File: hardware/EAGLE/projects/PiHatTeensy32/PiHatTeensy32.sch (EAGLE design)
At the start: 86 parts, among them IC2_0_PC JP, U0-C1 0.1uF, U0-C2 1nF, U0-C3 0.22uF, U0-C4 0.1uF, U0-C5 0.22uF, U0-R1 4.7k, U0-R2 47k, U0-R3 10k, U0-R4 10k, U1 TSR_1-2450, U1-C1 0.1uF, U1-C2 1nF, U1-C3 0.22uF, U1-C4 0.1uF, U1-C5 0.22uF, U1-R1 4.7k, U1-R2 47k, U1-R3 10k, U1-R4 10k, X1 RASPI_BOARD_B+_H

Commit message: teensy32 board added
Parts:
- removed H0-R1, H0-R2, H0-R3, H1-R1, H1-R2, H1-R3, U0-R3, U0-R4, U1-R3, U1-R4, V0-R3, V0-R4, V1-R3, V1-R4, W0-R3, W0-R4, W1-R3, W1-R4: 10k, SparkFun-Resistors:10KOHM-0603-1/10W-1%
- removed HALL0, HALL1: (no value), SparkFun-Connectors:CONN_06SMD-1MM
- removed HB-U0, HB-U1, HB-V0, HB-V1, HB-W0, HB-W1: (no value), ITX007T:IFX007TZZZZ
- removed I2C_1_IMU: JP, SparkFun-Connectors:CONN_041X04_NO_SILK
- removed IC2_0_PC, MOTOR0, MOTOR1, SERVO_0, SERVO_1: JP, SparkFun-Connectors:CONN_031X03_NO_SILK
- removed SPI_CONN0: ENCODER0, SparkFun-Connectors:CONN_06SMD-1MM
- removed SPI_CONN1: ENCODER1, SparkFun-Connectors:CONN_06SMD-1MM
- removed U0-C1, U0-C4, U1-C1, U1-C4, V0-C1, V0-C4, V1-C1, V1-C4, W0-C1, W0-C4, W1-C1, W1-C4: 0.1uF, SparkFun-Capacitors:0.1UF-0603-25V-5%
- removed U0-C2, U1-C2, V0-C2, V1-C2, W0-C2, W1-C2: 1nF, SparkFun-Capacitors:1.0NF/1000PF-0603-50V-10%
- removed U0-C3, U0-C5, U1-C3, U1-C5, V0-C3, V0-C5, V1-C3, V1-C5, W0-C3, W0-C5, W1-C3, W1-C5: 0.22uF, SparkFun-Capacitors:0.22UF-0603-25V-10%
- removed U0-R1, U1-R1, V0-R1, V1-R1, W0-R1, W1-R1: 4.7k, SparkFun-Resistors:4.7KOHM-0603-1/10W-1%
- removed U0-R2, U1-R2, V0-R2, V1-R2, W0-R2, W1-R2: 47k, SparkFun-Resistors:47KOHM-0603-1/10W-1%
- added U$1: TEENSY_3.1-3.2_ALL_PINS&PADS, Teensy_3_and_LC_Series_Boards_v1.4:TEENSY_3.1-3.2_ALL_PINS&PADS
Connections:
- removed net HB_INH_U0: HB-U0.INH, U0-R3.1
- removed net HB_INH_U1: HB-U1.INH, U1-R3.1
- removed net HB_INH_V0: HB-V0.INH, V0-R3.1
- removed net HB_INH_V1: HB-V1.INH, V1-R3.1
- removed net HB_INH_W0: HB-W0.INH, W0-R3.1
- removed net HB_INH_W1: HB-W1.INH, W1-R3.1
- removed net HB_IN_U0: HB-U0.IN, U0-R4.1
- removed net HB_IN_U1: HB-U1.IN, U1-R4.1
- removed net HB_IN_V0: HB-V0.IN, V0-R4.1
- removed net HB_IN_V1: HB-V1.IN, V1-R4.1
- removed net HB_IN_W0: HB-W0.IN, W0-R4.1
- removed net HB_IN_W1: HB-W1.IN, W1-R4.1
- removed net SR_U0: HB-U0.SR, U0-C2.2, U0-R2.2
- removed net SR_U1: HB-U1.SR, U1-C2.2, U1-R2.2
- removed net SR_V0: HB-V0.SR, V0-C2.2, V0-R2.2
- removed net SR_V1: HB-V1.SR, V1-C2.2, V1-R2.2
- removed net SR_W0: HB-W0.SR, W0-C2.2, W0-R2.2
- removed net SR_W1: HB-W1.SR, W1-C2.2, W1-R2.2
- removed net U0: HB-U0.OUT, MOTOR0.1, U0-C3.2, U0-C5.2
- removed net U1: HB-U1.OUT, MOTOR1.1, U1-C3.2, U1-C5.2
- removed net V0: HB-V0.OUT, MOTOR0.2, V0-C3.2, V0-C5.2
- removed net V1: HB-V1.OUT, MOTOR1.2, V1-C3.2, V1-C5.2
- removed net W0: HB-W0.OUT, MOTOR0.3, W0-C3.2, W0-C5.2
- removed net W1: HB-W1.OUT, MOTOR1.3, W1-C3.2, W1-C5.2
- net 3.3V: now also U$1.3.3V; no longer H0-R1.2, H0-R2.2, H0-R3.2, H1-R1.2, H1-R2.2, H1-R3.2, HALL0.6, HALL1.6, I2C_1_IMU.4, SPI_CONN0.5, SPI_CONN1.5
- net 5.0V: now also U$1.VIN, U1.VO
- net GND: now also U$1.GND; no longer HALL0.1, HALL1.1, HB-U0.GND, HB-U1.GND, HB-V0.GND, HB-V1.GND, HB-W0.GND, HB-W1.GND, I2C_1_IMU.1, IC2_0_PC.3, SERVO_0.1, SERVO_1.1, SPI_CONN0.6, SPI_CONN1.6, U0-C1.1, U0-C2.1, U0-C3.1, U0-C4.1, U0-R1.1, U0-R2.1, U1-C1.1, U1-C2.1, U1-C3.1, U1-C4.1, U1-R1.1, U1-R2.1, V0-C1.1, V0-C2.1, V0-C3.1, V0-C4.1, V0-R1.1, V0-R2.1, V1-C1.1, V1-C2.1, V1-C3.1, V1-C4.1, V1-R1.1, V1-R2.1, W0-C1.1, W0-C2.1, W0-C3.1, W0-C4.1, W0-R1.1, W0-R2.1, W1-C1.1, W1-C2.1, W1-C3.1, W1-C4.1, W1-R1.1, W1-R2.1
- net HALL_U0: no longer H0-R1.1, HALL0.4
- net HALL_U1: no longer H1-R1.1, HALL1.4
- net HALL_V0: no longer H0-R2.1, HALL0.3
- net HALL_V1: no longer H1-R2.1, HALL1.3
- net HALL_W0: no longer H0-R3.1, HALL0.2
- net HALL_W1: no longer H1-R3.1, HALL1.2
- net I2C0_SCL: no longer IC2_0_PC.2
- net I2C0_SDA: no longer IC2_0_PC.1
- net I2C1_SCL: no longer I2C_1_IMU.2
- net I2C1_SDA: no longer I2C_1_IMU.3
- net INH_U0: no longer U0-R3.2
- net INH_U1: no longer U1-R3.2
- net INH_V0: no longer V0-R3.2
- net INH_V1: no longer V1-R3.2
- net INH_W0: no longer W0-R3.2
- net INH_W1: no longer W1-R3.2
- net IN_U0: no longer U0-R4.2
- net IN_U1: no longer U1-R4.2
- net IN_V0: no longer V0-R4.2
- net IN_V1: no longer V1-R4.2
- net IN_W0: no longer W0-R4.2
- net IN_W1: no longer W1-R4.2
- net IS_U0: no longer HB-U0.IS, U0-C1.2, U0-R1.2
- net IS_U1: no longer HB-U1.IS, U1-C1.2, U1-R1.2
- net IS_V0: no longer HB-V0.IS, V0-C1.2, V0-R1.2
- net IS_V1: no longer HB-V1.IS, V1-C1.2, V1-R1.2
- net IS_W0: no longer HB-W0.IS, W0-C1.2, W0-R1.2
- net IS_W1: no longer HB-W1.IS, W1-C1.2, W1-R1.2
- net SERVO_0: no longer SERVO_0.2
- net SERVO_1: no longer SERVO_1.2
- net SPI_CS0: no longer SPI_CONN0.1
- net SPI_CS1: no longer SPI_CONN1.1
- net SPI_MISO: no longer SPI_CONN0.4, SPI_CONN1.4
- net SPI_MOSI: no longer SPI_CONN0.3, SPI_CONN1.3
- net SPI_SCLK: no longer SPI_CONN0.2, SPI_CONN1.2
- net VCC-SERVOS: no longer SERVO_0.3, SERVO_1.3, U1.VO
- net VI: no longer HB-U0.VS, HB-U1.VS, HB-V0.VS, HB-V1.VS, HB-W0.VS, HB-W1.VS, U0-C4.2, U0-C5.1, U1-C4.2, U1-C5.1, V0-C4.2, V0-C5.1, V1-C4.2, V1-C5.1, W0-C4.2, W0-C5.1, W1-C4.2, W1-C5.1
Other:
- moved on the sheet: MOTOR0_CONTROL, MOTOR0_SENS, MOTOR1_CONTROL, MOTOR1_SENS, VCC

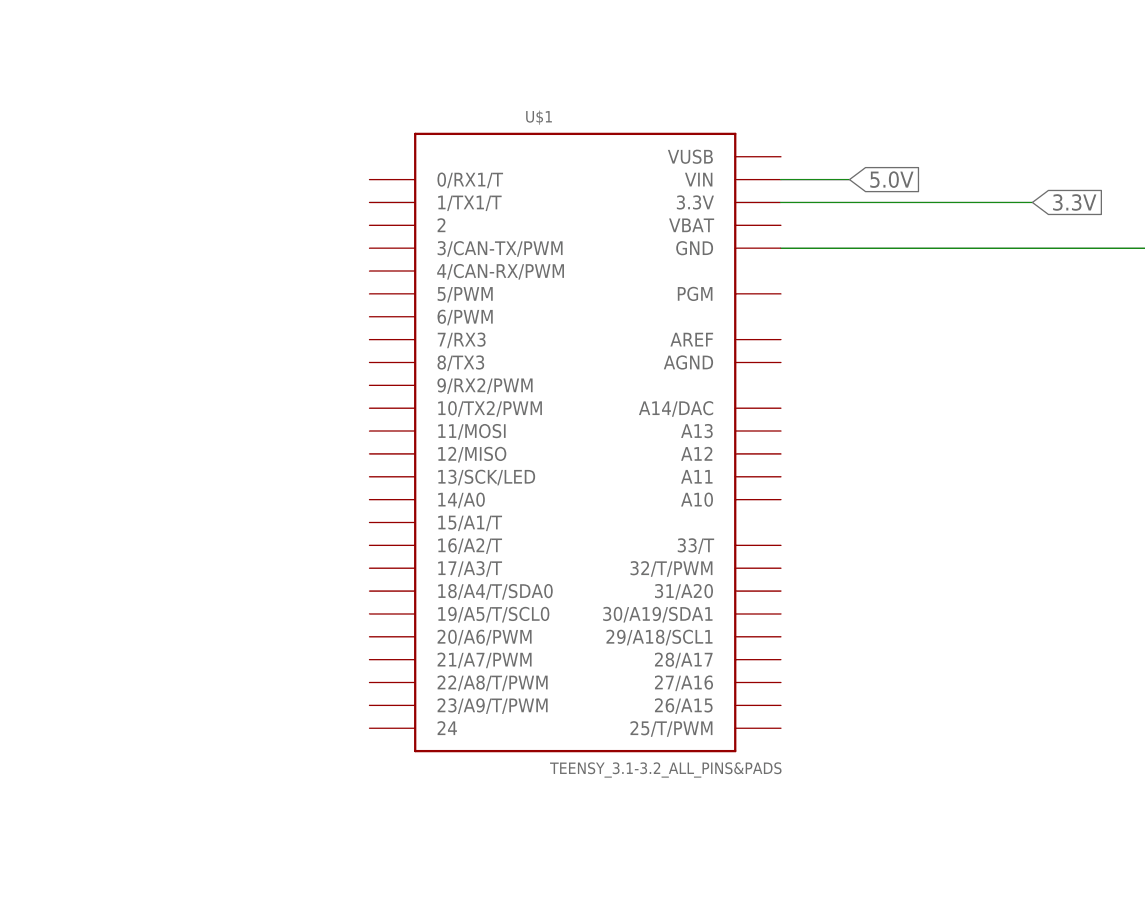
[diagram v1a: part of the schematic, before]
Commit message: schematic connection done, pins 16-17 should be wired to UART
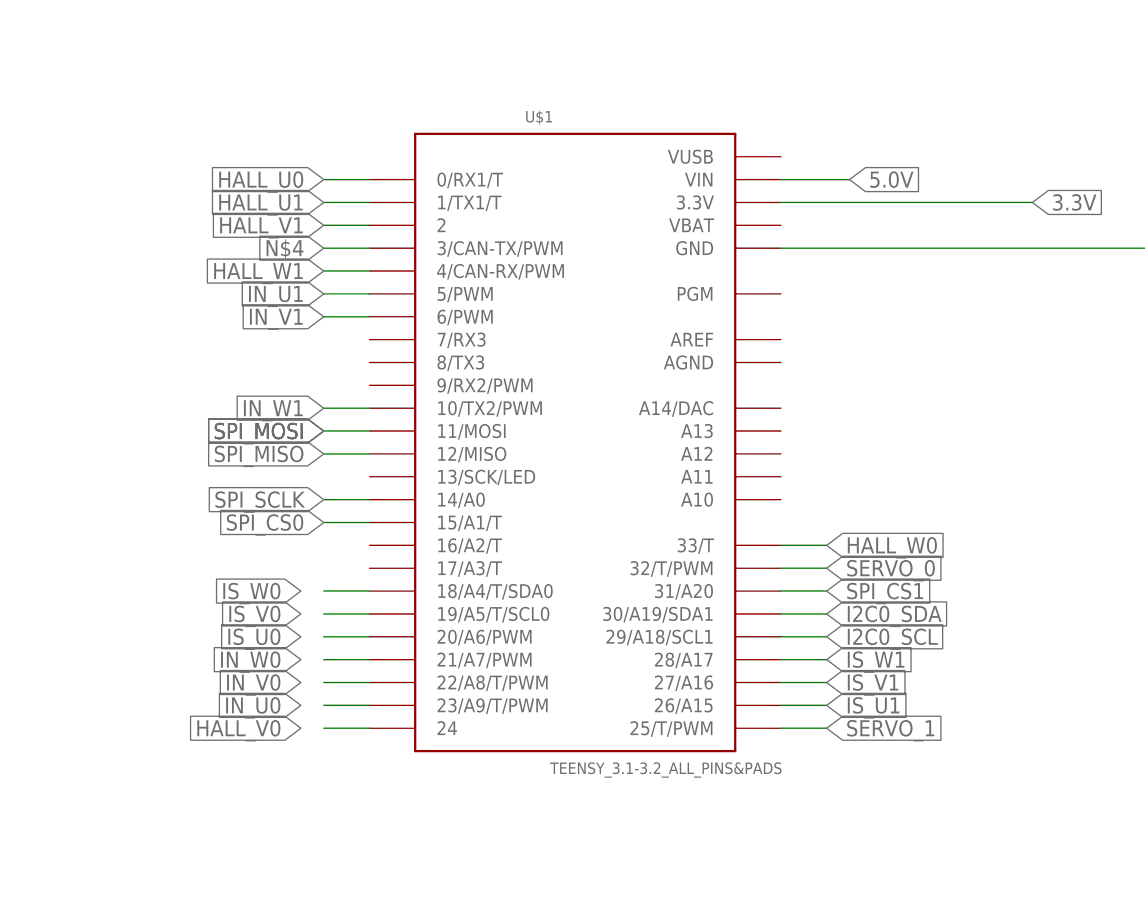
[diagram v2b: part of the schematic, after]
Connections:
- new net N$4: U$1.3/CAN-TX/PWM
- net HALL_U0: now also U$1.0/RX1/T
- net HALL_U1: now also U$1.1/TX1/T
- net HALL_V0: now also U$1.24
- net HALL_V1: now also U$1.2
- net HALL_W0: now also U$1.33/T
- net HALL_W1: now also U$1.4/CAN-RX/PWM
- net I2C0_SCL: now also U$1.29/A18/SCL1
- net I2C0_SDA: now also U$1.30/A19/SDA1
- net IN_U0: now also U$1.23/A9/T/PWM
- net IN_U1: now also U$1.5/PWM
- net IN_V0: now also U$1.22/A8/T/PWM
- net IN_V1: now also U$1.6/PWM
- net IN_W0: now also U$1.21/A7/PWM
- net IN_W1: now also U$1.10/TX2/PWM
- net IS_U0: now also U$1.20/A6/PWM
- net IS_U1: now also U$1.26/A15
- net IS_V0: now also U$1.19/A5/T/SCL0
- net IS_V1: now also U$1.27/A16
- net IS_W0: now also U$1.18/A4/T/SDA0
- net IS_W1: now also U$1.28/A17
- net SERVO_0: now also U$1.32/T/PWM
- net SERVO_1: now also U$1.25/T/PWM
- net SPI_CS0: now also U$1.15/A1/T
- net SPI_CS1: now also U$1.31/A20
- net SPI_MISO: now also U$1.12/MISO
- net SPI_MOSI: now also U$1.11/MOSI
- net SPI_SCLK: now also U$1.14/A0
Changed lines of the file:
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@@
 <?xml version="1.0" encoding="utf-8"?>
 <!DOCTYPE eagle SYSTEM "eagle.dtd">
-<eagle version="9.6.0">
+<eagle version="9.5.2">
 <drawing>
 <settings>
@@
 <pinref part="MOTOR0_CONTROL" gate="G$1" pin="4"/>
 </segment>
+<segment>
+<pinref part="U$1" gate="G$1" pin="23/A9/T/PWM"/>
+<wire x1="134.62" y1="-12.7" x2="129.54" y2="-12.7" width="0.1524" layer="91"/>
+<label x="127" y="-12.7" size="1.778" layer="95" rot="R180" xref="yes"/>
+</segment>
 </net>
 <net name="IN_V0" class="0">
@@
 <pinref part="MOTOR0_CONTROL" gate="G$1" pin="5"/>
 </segment>
+<segment>
+<pinref part="U$1" gate="G$1" pin="22/A8/T/PWM"/>
+<wire x1="134.62" y1="-10.16" x2="129.54" y2="-10.16" width="0.1524" layer="91"/>
+<label x="127" y="-10.16" size="1.778" layer="95" rot="R180" xref="yes"/>
+</segment>
 </net>
 <net name="IN_W0" class="0">
@@
 <pinref part="MOTOR0_CONTROL" gate="G$1" pin="6"/>
 </segment>
+<segment>
+<pinref part="U$1" gate="G$1" pin="21/A7/PWM"/>
+<wire x1="134.62" y1="-7.62" x2="129.54" y2="-7.62" width="0.1524" layer="91"/>
+<label x="127" y="-7.62" size="1.778" layer="95" rot="R180" xref="yes"/>
+</segment>
 </net>
 <net name="INH_U0" class="0">
@@
 <pinref part="MOTOR0_SENS" gate="G$1" pin="6"/>
 </segment>
+<segment>
+<pinref part="U$1" gate="G$1" pin="18/A4/T/SDA0"/>
+<wire x1="134.62" y1="0" x2="129.54" y2="0" width="0.1524" layer="91"/>
+<label x="127" y="0" size="1.778" layer="95" rot="R180" xref="yes"/>
+</segment>
 </net>
 <net name="IS_V0" class="0">
@@
 <pinref part="MOTOR0_SENS" gate="G$1" pin="5"/>
 </segment>
+<segment>
+<pinref part="U$1" gate="G$1" pin="19/A5/T/SCL0"/>
+<wire x1="134.62" y1="-2.54" x2="129.54" y2="-2.54" width="0.1524" layer="91"/>
+<label x="127" y="-2.54" size="1.778" layer="95" rot="R180" xref="yes"/>
+</segment>
 </net>
 <net name="IS_U0" class="0">
@@
 <label x="17.78" y="-15.24" size="1.778" layer="95" xref="yes"/>
 <pinref part="MOTOR0_SENS" gate="G$1" pin="4"/>
+</segment>
+<segment>
+<pinref part="U$1" gate="G$1" pin="20/A6/PWM"/>
+<wire x1="134.62" y1="-5.08" x2="129.54" y2="-5.08" width="0.1524" layer="91"/>
+<label x="127" y="-5.08" size="1.778" layer="95" rot="R180" xref="yes"/>
 </segment>
 </net>
@@
 <pinref part="MOTOR1_CONTROL" gate="G$1" pin="4"/>
 </segment>
+<segment>
+<pinref part="U$1" gate="G$1" pin="5/PWM"/>
+<wire x1="134.62" y1="33.02" x2="129.54" y2="33.02" width="0.1524" layer="91"/>
+<label x="129.54" y="33.02" size="1.778" layer="95" rot="R180" xref="yes"/>
+</segment>
 </net>
 <net name="IN_V1" class="0">
@@
 <pinref part="MOTOR1_CONTROL" gate="G$1" pin="5"/>
 </segment>
+<segment>
+<pinref part="U$1" gate="G$1" pin="6/PWM"/>
+<wire x1="134.62" y1="30.48" x2="129.54" y2="30.48" width="0.1524" layer="91"/>
+<label x="129.54" y="30.48" size="1.778" layer="95" rot="R180" xref="yes"/>
+</segment>
 </net>
 <net name="IN_W1" class="0">
@@
 <pinref part="MOTOR1_CONTROL" gate="G$1" pin="6"/>
 </segment>
+<segment>
+<pinref part="U$1" gate="G$1" pin="10/TX2/PWM"/>
+<wire x1="134.62" y1="20.32" x2="129.54" y2="20.32" width="0.1524" layer="91"/>
+<label x="129.54" y="20.32" size="1.778" layer="95" rot="R180" xref="yes"/>
+</segment>
 </net>
 <net name="INH_V1" class="0">
@@
 <pinref part="MOTOR1_SENS" gate="G$1" pin="6"/>
 </segment>
+<segment>
+<pinref part="U$1" gate="G$1" pin="28/A17"/>
+<wire x1="180.34" y1="-7.62" x2="185.42" y2="-7.62" width="0.1524" layer="91"/>
+<label x="185.42" y="-7.62" size="1.778" layer="95" xref="yes"/>
+</segment>
 </net>
 <net name="IS_V1" class="0">
@@
 <pinref part="MOTOR1_SENS" gate="G$1" pin="5"/>
 </segment>
+<segment>
+<pinref part="U$1" gate="G$1" pin="27/A16"/>
+<wire x1="180.34" y1="-10.16" x2="185.42" y2="-10.16" width="0.1524" layer="91"/>
+<label x="185.42" y="-10.16" size="1.778" layer="95" xref="yes"/>
+</segment>
 </net>
 <net name="IS_U1" class="0">
@@
 <pinref part="MOTOR1_SENS" gate="G$1" pin="4"/>
 </segment>
+<segment>
+<pinref part="U$1" gate="G$1" pin="26/A15"/>
+<wire x1="180.34" y1="-12.7" x2="185.42" y2="-12.7" width="0.1524" layer="91"/>
+<label x="185.42" y="-12.7" size="1.778" layer="95" xref="yes"/>
+</segment>
 </net>
 <net name="I2C1_SDA" class="0">
@@
 <label x="134.62" y="-114.3" size="1.778" layer="95" rot="R180" xref="yes"/>
 </segment>
+<segment>
+<pinref part="U$1" gate="G$1" pin="30/A19/SDA1"/>
+<wire x1="180.34" y1="-2.54" x2="185.42" y2="-2.54" width="0.1524" layer="91"/>
+<label x="185.42" y="-2.54" size="1.778" layer="95" xref="yes"/>
+</segment>
 </net>
 <net name="I2C0_SCL" class="0">
@@
 <label x="116.84" y="-111.76" size="1.778" layer="95" rot="R180" xref="yes"/>
 </segment>
+<segment>
+<pinref part="U$1" gate="G$1" pin="29/A18/SCL1"/>
+<wire x1="180.34" y1="-5.08" x2="185.42" y2="-5.08" width="0.1524" layer="91"/>
+<label x="185.42" y="-5.08" size="1.778" layer="95" xref="yes"/>
+</segment>
 </net>
 <net name="SPI_SCLK" class="0">
@@
 <label x="187.96" y="-68.58" size="1.778" layer="95" xref="yes"/>
 </segment>
+<segment>
+<pinref part="U$1" gate="G$1" pin="14/A0"/>
+<wire x1="134.62" y1="10.16" x2="129.54" y2="10.16" width="0.1524" layer="91"/>
+<label x="129.54" y="10.16" size="1.778" layer="95" rot="R180" xref="yes"/>
+</segment>
 </net>
 <net name="SPI_MOSI" class="0">
@@
 <label x="187.96" y="-63.5" size="1.778" layer="95" xref="yes"/>
 </segment>
+<segment>
+<pinref part="U$1" gate="G$1" pin="11/MOSI"/>
+<wire x1="134.62" y1="17.78" x2="129.54" y2="17.78" width="0.1524" layer="91"/>
+<label x="129.54" y="17.78" size="1.778" layer="95" rot="R180" xref="yes"/>
+<label x="129.54" y="17.78" size="1.778" layer="95" rot="R180" xref="yes"/>
+</segment>
 </net>
 <net name="SPI_MISO" class="0">
@@
 <label x="187.96" y="-66.04" size="1.778" layer="95" xref="yes"/>
 </segment>
+<segment>
+<pinref part="U$1" gate="G$1" pin="12/MISO"/>
+<wire x1="134.62" y1="15.24" x2="129.54" y2="15.24" width="0.1524" layer="91"/>
+<label x="129.54" y="15.24" size="1.778" layer="95" rot="R180" xref="yes"/>
+</segment>
 </net>
 <net name="SPI_CS1" class="0">
@@
 <label x="187.96" y="-73.66" size="1.778" layer="95" xref="yes"/>
 </segment>
+<segment>
+<pinref part="U$1" gate="G$1" pin="31/A20"/>
+<wire x1="180.34" y1="0" x2="185.42" y2="0" width="0.1524" layer="91"/>
+<label x="185.42" y="0" size="1.778" layer="95" xref="yes"/>
+</segment>
 </net>
 <net name="SPI_CS0" class="0">
@@
 <label x="187.96" y="-71.12" size="1.778" layer="95" xref="yes"/>
 </segment>
+<segment>
+<pinref part="U$1" gate="G$1" pin="15/A1/T"/>
+<wire x1="134.62" y1="7.62" x2="129.54" y2="7.62" width="0.1524" layer="91"/>
+<label x="129.54" y="7.62" size="1.778" layer="95" rot="R180" xref="yes"/>
+</segment>
 </net>
 <net name="HALL_U0" class="0">
@@
 <pinref part="MOTOR0_SENS" gate="G$1" pin="1"/>
 </segment>
+<segment>
+<pinref part="U$1" gate="G$1" pin="0/RX1/T"/>
+<wire x1="134.62" y1="45.72" x2="129.54" y2="45.72" width="0.1524" layer="91"/>
+<label x="129.54" y="45.72" size="1.778" layer="95" rot="R180" xref="yes"/>
+</segment>
 </net>
 <net name="HALL_V0" class="0">
@@
 <pinref part="MOTOR0_SENS" gate="G$1" pin="2"/>
 </segment>
+<segment>
+<pinref part="U$1" gate="G$1" pin="24"/>
+<wire x1="134.62" y1="-15.24" x2="129.54" y2="-15.24" width="0.1524" layer="91"/>
+<label x="127" y="-15.24" size="1.778" layer="95" rot="R180" xref="yes"/>
+</segment>
 </net>
 <net name="HALL_W0" class="0">
@@
 <pinref part="MOTOR0_SENS" gate="G$1" pin="3"/>
 </segment>
+<segment>
+<pinref part="U$1" gate="G$1" pin="33/T"/>
+<wire x1="180.34" y1="5.08" x2="185.42" y2="5.08" width="0.1524" layer="91"/>
+<label x="185.42" y="5.08" size="1.778" layer="95" xref="yes"/>
+</segment>
 </net>
 <net name="SERVO_0" class="0">
@@
 <pinref part="SERVOS" gate="G$1" pin="1"/>
 </segment>
+<segment>
+<pinref part="U$1" gate="G$1" pin="32/T/PWM"/>
+<wire x1="180.34" y1="2.54" x2="185.42" y2="2.54" width="0.1524" layer="91"/>
+<label x="185.42" y="2.54" size="1.778" layer="95" xref="yes"/>
+</segment>
 </net>
 <net name="HALL_U1" class="0">
@@
 <pinref part="MOTOR1_SENS" gate="G$1" pin="1"/>
 </segment>
+<segment>
+<pinref part="U$1" gate="G$1" pin="1/TX1/T"/>
+<wire x1="134.62" y1="43.18" x2="129.54" y2="43.18" width="0.1524" layer="91"/>
+<label x="129.54" y="43.18" size="1.778" layer="95" rot="R180" xref="yes"/>
+</segment>
 </net>
 <net name="HALL_V1" class="0">
@@
 <pinref part="MOTOR1_SENS" gate="G$1" pin="2"/>
 </segment>
+<segment>
+<pinref part="U$1" gate="G$1" pin="2"/>
+<wire x1="134.62" y1="40.64" x2="129.54" y2="40.64" width="0.1524" layer="91"/>
+<label x="129.54" y="40.64" size="1.778" layer="95" rot="R180" xref="yes"/>
+</segment>
 </net>
 <net name="HALL_W1" class="0">
@@
 <pinref part="MOTOR1_SENS" gate="G$1" pin="3"/>
 </segment>
+<segment>
+<pinref part="U$1" gate="G$1" pin="4/CAN-RX/PWM"/>
+<wire x1="134.62" y1="35.56" x2="129.54" y2="35.56" width="0.1524" layer="91"/>
+<label x="129.54" y="35.56" size="1.778" layer="95" rot="R180" xref="yes"/>
+</segment>
 </net>
 <net name="SERVO_1" class="0">
@@
 <pinref part="SERVOS" gate="G$1" pin="2"/>
 </segment>
+<segment>
+<pinref part="U$1" gate="G$1" pin="25/T/PWM"/>
+<wire x1="180.34" y1="-15.24" x2="185.42" y2="-15.24" width="0.1524" layer="91"/>
+<label x="185.42" y="-15.24" size="1.778" layer="95" xref="yes"/>
+</segment>
 </net>
 <net name="5.0V" class="0">
@@
 </segment>
 </net>
+<net name="N$4" class="0">
+<segment>
+<pinref part="U$1" gate="G$1" pin="3/CAN-TX/PWM"/>
+<wire x1="134.62" y1="38.1" x2="129.54" y2="38.1" width="0.1524" layer="91"/>
+<label x="129.54" y="38.1" size="1.778" layer="95" rot="R180" xref="yes"/>
+</segment>
+</net>

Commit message: PiHat update
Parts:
- added T4: BM08B-SRSS-TB, con-jst2:BM08B-SRSS-TB
- added T4-24-25, T4-30-31, T4-32-33: (no value), SparkFun-Connectors:CONN_021X02_NO_SILK
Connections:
- removed net HALL_U0: MOTOR0_SENS.1, U$1.0/RX1/T
- removed net HALL_W0: MOTOR0_SENS.3, U$1.33/T
- removed net HALL_W1: MOTOR1_SENS.3, U$1.4/CAN-RX/PWM
- removed net I2C1_SCL: X1.ID_SC
- removed net I2C1_SDA: X1.ID_SD
- removed net N$4: U$1.3/CAN-TX/PWM
- removed net SPI_CS1: U$1.31/A20, X1.SPI_CE1
- new net HALL_U0_&_I2C1_SCL: MOTOR0_SENS.1, T4-24-25.2, U$1.29/A18/SCL1, X1.ID_SC
- new net HALL_W0_&_I2C1_SDA: MOTOR0_SENS.3, U$1.30/A19/SDA1, X1.ID_SD
- new net PI_RX: U$1.1/TX1/T, X1.RXD
- new net PI_TX: U$1.0/RX1/T, X1.TXD
- new net SPI_CS1_&_HALL_W1: MOTOR1_SENS.3, U$1.14/A0, X1.SPI_CE1
- net HALL_U1: now also T4-32-33.1, U$1.24; no longer U$1.1/TX1/T
- net HALL_V0: now also T4-24-25.1, U$1.32/T/PWM; no longer U$1.24
- net HALL_V1: now also T4-30-31.1, U$1.25/T/PWM; no longer U$1.2
- net I2C0_SCL: now also U$1.19/A5/T/SCL0; no longer U$1.29/A18/SCL1
- net I2C0_SDA: now also U$1.18/A4/T/SDA0; no longer U$1.30/A19/SDA1
- net INH_U0: now also U$1.26/A15, U$1.7/RX3
- net INH_V0: now also T4-32-33.2, U$1.33/T
- net INH_V1: now also U$1.8/TX3
- net INH_W0: now also U$1.31/A20
- net INH_W1: now also T4-30-31.2, U$1.28/A17
- net IN_U0: now also T4-1.S
- net IN_U1: now also T4-6.S
- net IN_V0: now also T4-2.S
- net IN_V1: now also T4-7.S
- net IN_W0: now also T4-4.S, U$1.10/TX2/PWM; no longer U$1.21/A7/PWM
- net IN_W1: now also T4-8.S, U$1.9/RX2/PWM; no longer U$1.10/TX2/PWM
- net IS_U0: now also U$1.15/A1/T; no longer U$1.20/A6/PWM
- net IS_U1: now also U$1.27/A16; no longer U$1.26/A15
- net IS_V0: now also U$1.20/A6/PWM; no longer U$1.19/A5/T/SCL0
- net IS_V1: now also U$1.16/A2/T; no longer U$1.27/A16
- net IS_W0: now also U$1.21/A7/PWM; no longer U$1.18/A4/T/SDA0
- net IS_W1: now also U$1.17/A3/T; no longer U$1.28/A17
- net SERVO_0: now also U$1.3/CAN-TX/PWM; no longer U$1.32/T/PWM
- net SERVO_1: now also U$1.4/CAN-RX/PWM; no longer U$1.25/T/PWM
- net SPI_CS0: now also U$1.2; no longer U$1.15/A1/T
- net SPI_SCLK: now also U$1.13/SCK/LED; no longer U$1.14/A0
